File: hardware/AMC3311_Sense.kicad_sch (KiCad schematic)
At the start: 29 parts, among them U8 AMC3311QDWERQ1, U9 TLV9002QDRQ1

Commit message: updated TP
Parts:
- TP23, TP24, TP25, TP26: footprint LHRS_Special:TestPoint_HEX_3mmID -> TestPoint:TestPoint_THTPad_D3.0mm_Drill1.5mm
- renumbered C47 to C45, C45 to C46, C46 to C47

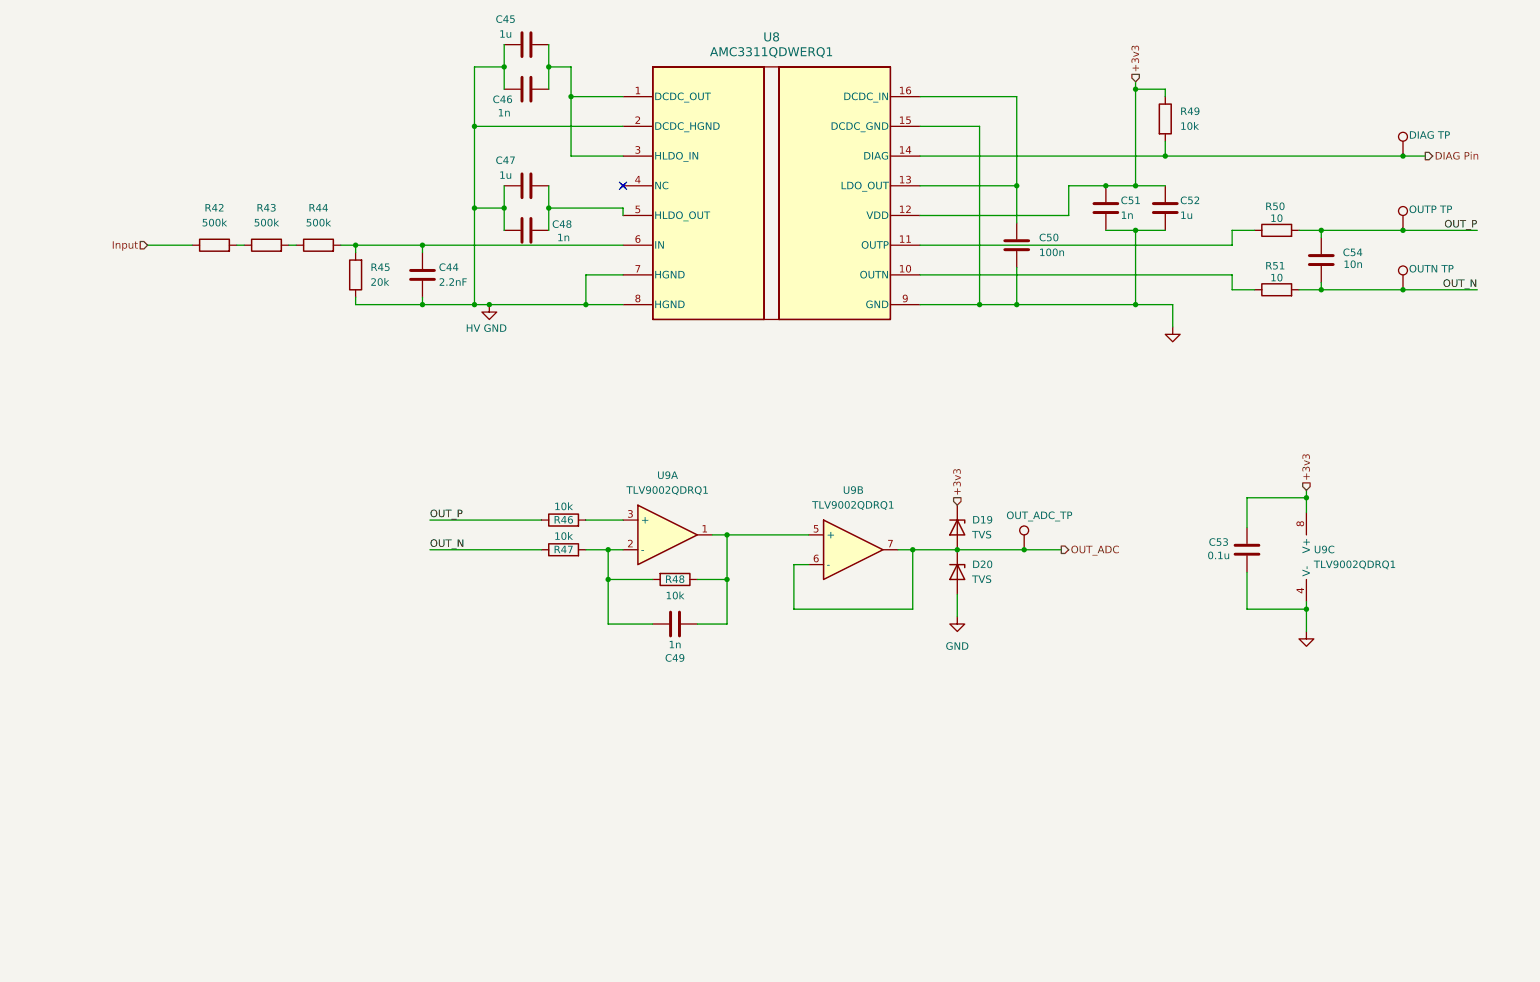
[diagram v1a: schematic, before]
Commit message: reduce op amps, better hierarchal
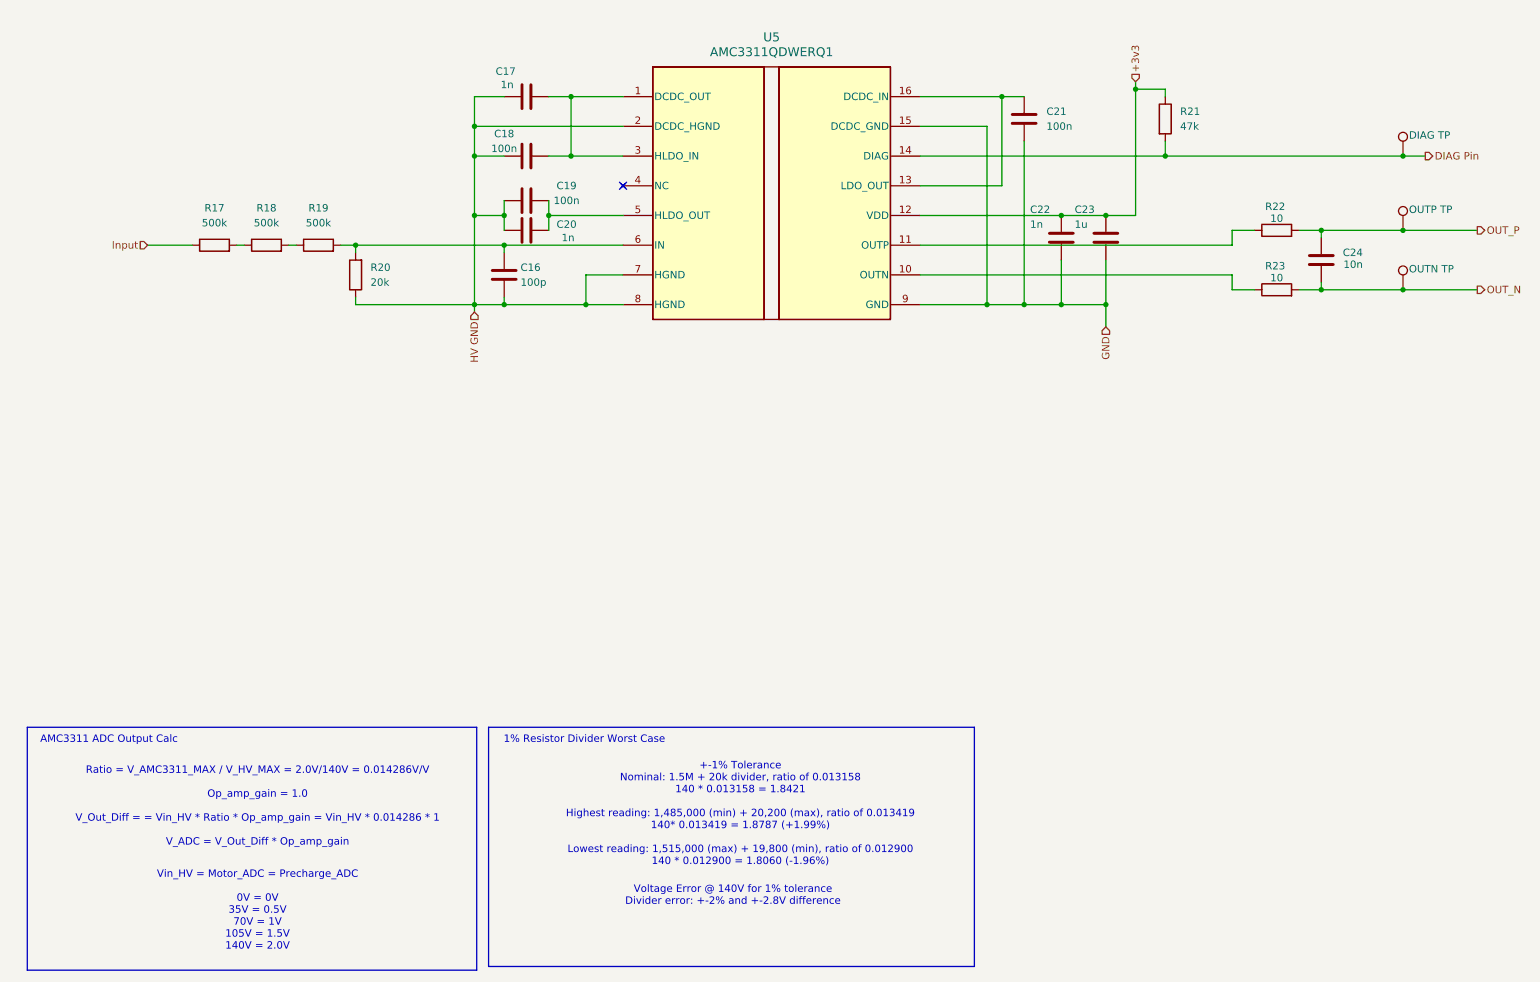
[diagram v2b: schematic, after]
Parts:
- removed C49: 1n, Capacitor_SMD:C_0603_1608Metric_Pad1.08x0.95mm_HandSolder, symbol Device:C
- removed C52: 1u, Capacitor_SMD:C_0603_1608Metric_Pad1.08x0.95mm_HandSolder, symbol Device:C
- removed C53: 0.1u, Capacitor_SMD:C_0603_1608Metric_Pad1.08x0.95mm_HandSolder, symbol Device:C
- removed D19, D20: TVS, Diode_SMD:D_SOD-123F, symbol Device:D_Zener
- removed R46, R47, R48: 10k, Resistor_SMD:R_0603_1608Metric_Pad0.98x0.95mm_HandSolder, symbol Device:R
- removed TP23: OUT_ADC_TP, TestPoint:TestPoint_THTPad_D3.0mm_Drill1.5mm, symbol Connector:TestPoint
- removed U9: TLV9002QDRQ1, Package_SO:SOIC-8_3.9x4.9mm_P1.27mm, symbol lhrs_misc:TLV9002QDRQ1
- added C23: 1u, Capacitor_SMD:C_0603_1608Metric_Pad1.08x0.95mm_HandSolder, symbol Device:C
- C16: renamed from C44; value 2.2nF -> 100p
- C18: renamed from C45; value 1u -> 100n
- C19: renamed from C47; value 1u -> 100n
- R21: renamed from R49; value 10k -> 47k
- renumbered C46 to C17, C48 to C20, C50 to C21, C51 to C22, C54 to C24, R42 to R17, R43 to R18, R44 to R19, R45 to R20, R50 to R22, R51 to R23, TP24 to TP7, TP25 to TP8, TP26 to TP9, U8 to U5
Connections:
- net +3v3: now also C23.1
- net GND: now also C23.2
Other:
- note added: "+-1% Tolerance Nominal: 1.5M + 20k divider, ratio of 0.013158 140 * 0.013158 = 1.8421 Highest reading: 1,485,000 (min) + 20,200 (max), ratio of 0.013419 140* 0.013419 = 1.8787 (+1.99%) Lowest reading: 1,515,000 (max) + 19,800 (min), ratio of 0.012900 140 * 0.012900 = 1.8060 (-1.96%)"
- note added: "1% Resistor Divider Worst Case"
- note added: "AMC3311 ADC Output Calc"
- note added: "Ratio = V_AMC3311_MAX / V_HV_MAX = 2.0V/140V = 0.014286V/V Op_amp_gain = 1.0 V_Out_Diff = = Vin_HV * Ratio * Op_amp_gain = Vin_HV * 0.014286 * 1 V_ADC = V_Out_Diff * Op_amp_gain"
- note added: "Vin_HV = Motor_ADC = Precharge_ADC 0V = 0V 35V = 0.5V 70V = 1V 105V = 1.5V 140V = 2.0V"
- note added: "Voltage Error @ 140V for 1% tolerance Divider error: +-2% and +-2.8V difference"
- moved on the sheet: C16, C17, C18, C19, C21, C22

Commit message: added outside test points, removed unncessary symbol fields
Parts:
- removed TP7: DIAG TP, TestPoint:TestPoint_THTPad_D3.0mm_Drill1.5mm, symbol Connector:TestPoint
- removed TP8: OUTP TP, TestPoint:TestPoint_THTPad_D3.0mm_Drill1.5mm, symbol Connector:TestPoint
- removed TP9: OUTN TP, TestPoint:TestPoint_THTPad_D3.0mm_Drill1.5mm, symbol Connector:TestPoint

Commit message: updated kicad sharepoint, added pn
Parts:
- C16: P/N (none) -> MMARQ167SCG101JTRA18
- C17, C20, C22: P/N (none) -> UMK107B7102MAHT
- C18, C19, C21: P/N (none) -> MAJCH168BB7104KTEA01
- C23: P/N (none) -> MLASU168SB5105KTNA01
- C24: P/N (none) -> EMK107SD103KA-T
- R21: P/N (none) -> CRCW060347K0FKECC
- R22, R23: P/N (none) -> CRCW060310R0FKEE
- U5: P/N (none) -> AMC3311QDWERQ1

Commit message: updated PN
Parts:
- R17, R18, R19: P/N (none) -> RNCF0805BTE500K
- R20: footprint Resistor_SMD:R_0805_2012Metric_Pad1.20x1.40mm_HandSolder -> Resistor_SMD:R_0603_1608Metric_Pad0.98x0.95mm_HandSolder; P/N (none) -> CR0603-FX-2002ELF
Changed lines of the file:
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@@
+			)
+		)
+		(property "P/N" "RNCF0805BTE500K"
+			(at 45.72 72.39 90)
+			(hide yes)
+			(show_name no)
+			(do_not_autoplace no)
+			(effects
+				(font
+					(size 1.27 1.27)
+				)
 			)
 		)
@@
 			)
 		)
+		(property "P/N" "RNCF0805BTE500K"
+			(at 63.5 72.39 90)
+			(hide yes)
+			(show_name no)
+			(do_not_autoplace no)
+			(effects
+				(font
+					(size 1.27 1.27)
+				)
+			)
+		)
 		(pin "2"
 		)
@@
 			)
 		)
-		(property "Footprint" "Resistor_SMD:R_0805_2012Metric_Pad1.20x1.40mm_HandSolder"
+		(property "Footprint" "Resistor_SMD:R_0603_1608Metric_Pad0.98x0.95mm_HandSolder"
 			(at 71.628 77.47 90)
 			(hide yes)
@@
 		)
 		(property "Description" "Resistor"
+			(at 69.85 77.47 0)
+			(hide yes)
+			(show_name no)
+			(do_not_autoplace no)
+			(effects
+				(font
+					(size 1.27 1.27)
+				)
+			)
+		)
+		(property "P/N" "CR0603-FX-2002ELF "
 			(at 69.85 77.47 0)
 			(hide yes)
@@
 			(hide yes)
 			(show_name no)
+			(do_not_autoplace no)
+			(effects
+				(font
+					(size 1.27 1.27)
+				)
+			)
+		)
+		(property "P/N" "RNCF0805BTE500K"
+			(at 54.61 72.39 90)
+			(hide yes)
+			(show_name no)
